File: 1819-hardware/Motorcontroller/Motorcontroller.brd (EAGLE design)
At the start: 34.3 x 41.6 mm, 30 parts, among them J11 455-1750-1-ND, J8 455-1750-1-ND, U1 GENERIC-SOIC8MSGEQ7N-FILTER, U2 GENERIC-SOIC8MSGEQ7N-FILTER, U3 GENERIC-SOIC8MSGEQ7N-FILTER, U4 PCA9685, U5 GENERIC-SOIC8MSGEQ7N-FILTER

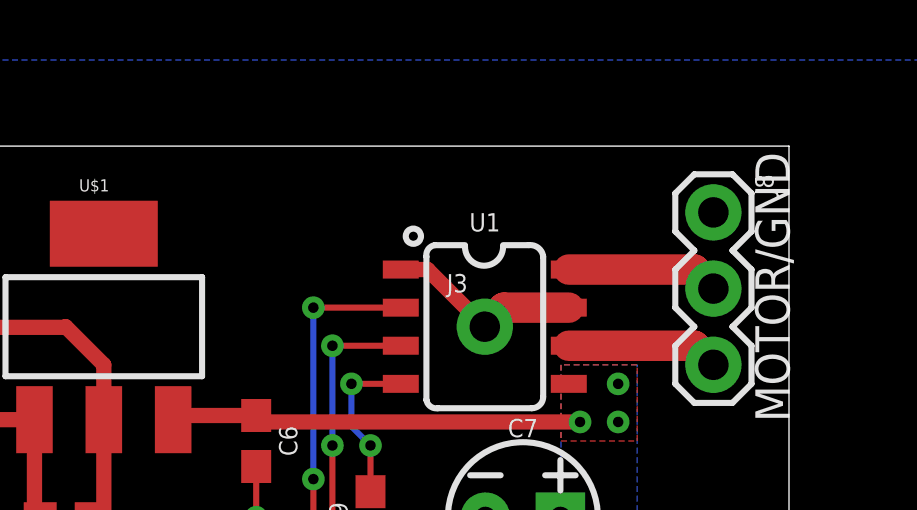
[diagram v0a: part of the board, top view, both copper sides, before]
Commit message: fixed pwm timing
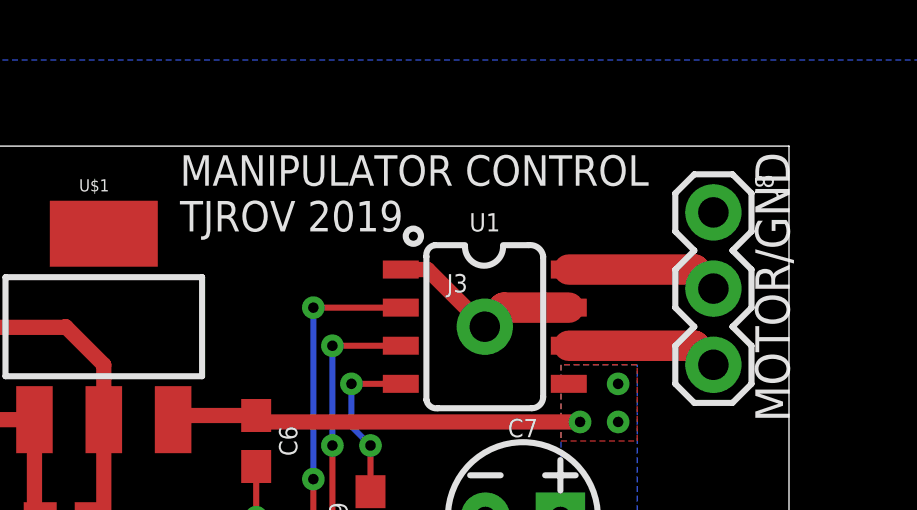
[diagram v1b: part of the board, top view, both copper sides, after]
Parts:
- moved FRAME1 60.5 mm to (0.00, 0.00)
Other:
- board text added: "MANIPULATOR CONTROL TJROV 2019"
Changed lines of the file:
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@@
 <text x="34.29" y="21.59" size="1.143" layer="21" font="vector" rot="R90">MOTOR</text>
 <text x="34.29" y="32.385" size="1.143" layer="21" font="vector" rot="R90">MOTOR/GND</text>
+<text x="13.97" y="38.735" size="1.016" layer="21" font="vector">MANIPULATOR CONTROL
+TJROV 2019</text>
 </plain>
 <attributes>
@@
 <attribute name="VALUE" x="25.4" y="26.543" size="0.6096" layer="27" font="vector" ratio="20" align="top-center"/>
 </element>
-<element name="FRAME1" library="SparkFun-Aesthetics" package="DUMMY" value="FRAME-LETTERNO_PACKAGE" x="-38.1" y="46.99">
-<attribute name="DESIGNER" value="Nobody" x="0" y="0" size="1.778" layer="27" display="off"/>
-<attribute name="VERSION" value="v01" x="0" y="0" size="1.778" layer="27" display="off"/>
+<element name="FRAME1" library="SparkFun-Aesthetics" package="DUMMY" value="FRAME-LETTERNO_PACKAGE" x="0" y="0">
+<attribute name="DESIGNER" value="Nobody" x="38.1" y="-46.99" size="1.778" layer="27" display="off"/>
+<attribute name="VERSION" value="v01" x="38.1" y="-46.99" size="1.778" layer="27" display="off"/>
 </element>
 <element name="J1" library="SparkFun-Connectors" package="1X08" value="" x="2.54" y="27.94" rot="R270">
@@
 </drawing>
 <compatibility>
+<note version="6.3" minversion="6.2.2" severity="warning">
+Since Version 6.2.2 text objects can contain more than one line,
+which will not be processed correctly with this version.
+</note>
 <note version="8.2" severity="warning">
 Since Version 8.2, EAGLE supports online libraries. The ids
